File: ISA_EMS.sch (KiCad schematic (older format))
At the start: 60 parts, among them J1 ISA BUS, J2 EMS Address, J3 ROM Config, U1 74HCT688, U10 74HCT32, U11 74HCT04, U12 74ACT245, U13 AS6C4008-55PCN, U14 AS6C4008-55PCN, U15 AS6C4008-55PCN, U16 AS6C4008-55PCN, U17 74HCT138, U18 74LS573, U19 74LS573, U2 SST39SF040, U20 74LS573, U21 74LS573, U3 AS6C4008-55PCN, U4 AS6C4008-55PCN, U5 AS6C4008-55PCN, U6 AS6C4008-55PCN, U7 74HCT688, U8 74HCT688, U9 74HCT139

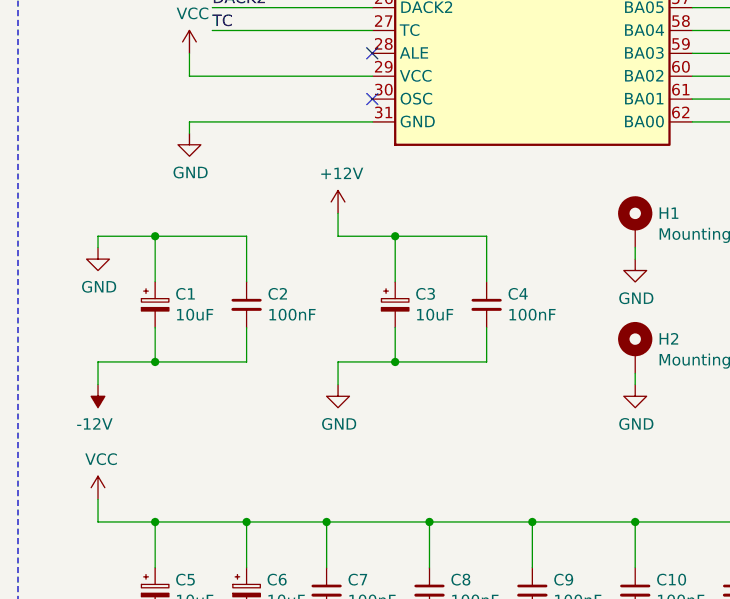
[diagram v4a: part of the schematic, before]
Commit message: Routed the board
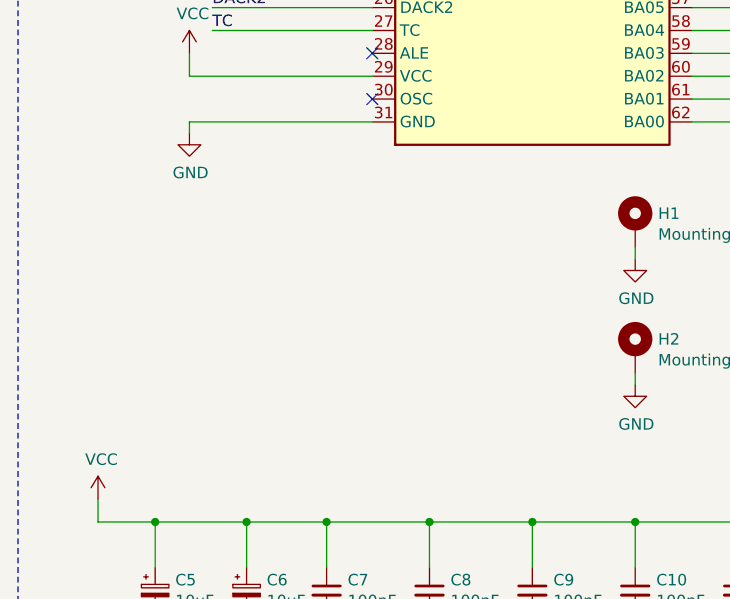
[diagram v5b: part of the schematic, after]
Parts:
- removed C1, C3: 10uF, Capacitor_THT:CP_Radial_D5.0mm_P2.50mm, symbol Device:CP_Small
- removed C2, C4: 100nF, Capacitor_THT:C_Disc_D6.0mm_W2.5mm_P5.00mm, symbol Device:C_Small
- H1, H2: footprint (none) -> skiselev_footprints:Hole_3mm
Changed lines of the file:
@@
 	1500 9250 2300 9250
 $Comp
-L Device:CP_Small C1
-U 1 1 610853FE
-P 1350 10250
-F 0 "C1" H 1438 10296 50  0000 L CNN
-F 1 "10uF" H 1438 10205 50  0000 L CNN
-F 2 "Capacitor_THT:CP_Radial_D5.0mm_P2.50mm" H 1350 10250 50  0001 C CNN
-F 3 "~" H 1350 10250 50  0001 C CNN
-	1    1350 10250
-	1    0    0    -1
-$EndComp
-$Comp
-L Device:C_Small C2
-U 1 1 61086024
-P 1750 10250
-F 0 "C2" H 1842 10296 50  0000 L CNN
-F 1 "100nF" H 1842 10205 50  0000 L CNN
-F 2 "Capacitor_THT:C_Disc_D6.0mm_W2.5mm_P5.00mm" H 1750 10250 50  0001 C CNN
-F 3 "~" H 1750 10250 50  0001 C CNN
-	1    1750 10250
-	1    0    0    -1
-$EndComp
-$Comp
-L power:GND #PWR0135
-U 1 1 6108687E
-P 1100 10000
-F 0 "#PWR0135" H 1100 9750 50  0001 C CNN
-F 1 "GND" H 1105 9827 50  0000 C CNN
-F 2 "" H 1100 10000 50  0001 C CNN
-F 3 "" H 1100 10000 50  0001 C CNN
-	1    1100 10000
-	1    0    0    -1
-$EndComp
-Wire Wire Line
-	1100 10000 1100 9950
-Wire Wire Line
-	1100 9950 1350 9950
-Wire Wire Line
-	1350 9950 1350 10150
-Wire Wire Line
-	1350 9950 1750 9950
-Wire Wire Line
-	1750 9950 1750 10150
-Connection ~ 1350 9950
-$Comp
-L power:-12V #PWR0136
-U 1 1 610C70C1
-P 1100 10600
-F 0 "#PWR0136" H 1100 10700 50  0001 C CNN
-F 1 "-12V" H 1115 10773 50  0000 C CNN
-F 2 "" H 1100 10600 50  0001 C CNN
-F 3 "" H 1100 10600 50  0001 C CNN
-	1    1100 10600
-	-1   0    0    1
-$EndComp
-Wire Wire Line
-	1750 10500 1350 10500
-Wire Wire Line
-	1350 10500 1350 10350
-Wire Wire Line
-	1750 10350 1750 10500
-Wire Wire Line
-	1350 10500 1100 10500
-Wire Wire Line
-	1100 10500 1100 10600
-Connection ~ 1350 10500
-$Comp
-L Device:CP_Small C3
-U 1 1 6116AF87
-P 2400 10250
-F 0 "C3" H 2488 10296 50  0000 L CNN
-F 1 "10uF" H 2488 10205 50  0000 L CNN
-F 2 "Capacitor_THT:CP_Radial_D5.0mm_P2.50mm" H 2400 10250 50  0001 C CNN
-F 3 "~" H 2400 10250 50  0001 C CNN
-	1    2400 10250
-	1    0    0    -1
-$EndComp
-$Comp
-L Device:C_Small C4
-U 1 1 6116B0B7
-P 2800 10250
-F 0 "C4" H 2892 10296 50  0000 L CNN
-F 1 "100nF" H 2892 10205 50  0000 L CNN
-F 2 "Capacitor_THT:C_Disc_D6.0mm_W2.5mm_P5.00mm" H 2800 10250 50  0001 C CNN
-F 3 "~" H 2800 10250 50  0001 C CNN
-	1    2800 10250
-	1    0    0    -1
-$EndComp
-$Comp
-L power:GND #PWR0137
-U 1 1 6116B0C1
-P 2150 10600
-F 0 "#PWR0137" H 2150 10350 50  0001 C CNN
-F 1 "GND" H 2155 10427 50  0000 C CNN
-F 2 "" H 2150 10600 50  0001 C CNN
-F 3 "" H 2150 10600 50  0001 C CNN
-	1    2150 10600
-	1    0    0    -1
-$EndComp
-Wire Wire Line
-	2400 9950 2400 10150
-Wire Wire Line
-	2400 9950 2800 9950
-Wire Wire Line
-	2800 9950 2800 10150
-Wire Wire Line
-	2800 10500 2400 10500
-Wire Wire Line
-	2400 10500 2400 10350
-Wire Wire Line
-	2800 10350 2800 10500
-Wire Wire Line
-	2400 10500 2150 10500
-Wire Wire Line
-	2150 10500 2150 10600
-Connection ~ 2400 10500
-Wire Wire Line
-	2400 9950 2150 9950
-Connection ~ 2400 9950
-Wire Wire Line
-	2150 9850 2150 9950
-$Comp
-L power:+12V #PWR0138
-U 1 1 61240CC5
-P 2150 9850
-F 0 "#PWR0138" H 2150 9700 50  0001 C CNN
-F 1 "+12V" H 2165 10023 50  0000 C CNN
-F 2 "" H 2150 9850 50  0001 C CNN
-F 3 "" H 2150 9850 50  0001 C CNN
-	1    2150 9850
-	1    0    0    -1
-$EndComp
-$Comp
 L Device:CP_Small C5
 U 1 1 61243061
@@
 F 0 "H1" H 3550 9949 50  0000 L CNN
 F 1 "MountingHole_Pad" H 3550 9858 50  0000 L CNN
-F 2 "" H 3450 9900 50  0001 C CNN
+F 2 "skiselev_footprints:Hole_3mm" H 3450 9900 50  0001 C CNN
 F 3 "~" H 3450 9900 50  0001 C CNN
 	1    3450 9900
@@
 F 0 "H2" H 3550 10499 50  0000 L CNN
 F 1 "MountingHole_Pad" H 3550 10408 50  0000 L CNN
-F 2 "" H 3450 10450 50  0001 C CNN
+F 2 "skiselev_footprints:Hole_3mm" H 3450 10450 50  0001 C CNN
 F 3 "~" H 3450 10450 50  0001 C CNN
 	1    3450 10450
@@
 $EndComp
 $Comp
-L power:GND #PWR?
+L power:GND #PWR0173
 U 1 1 60A008FD
 P 3450 10050
-F 0 "#PWR?" H 3450 9800 50  0001 C CNN
+F 0 "#PWR0173" H 3450 9800 50  0001 C CNN
 F 1 "GND" H 3455 9877 50  0000 C CNN
 F 2 "" H 3450 10050 50  0001 C CNN
@@
 $EndComp
 $Comp
-L power:GND #PWR?
+L power:GND #PWR0174
 U 1 1 60A01C8A
 P 3450 10600
-F 0 "#PWR?" H 3450 10350 50  0001 C CNN
+F 0 "#PWR0174" H 3450 10350 50  0001 C CNN
 F 1 "GND" H 3455 10427 50  0000 C CNN
 F 2 "" H 3450 10600 50  0001 C CNN

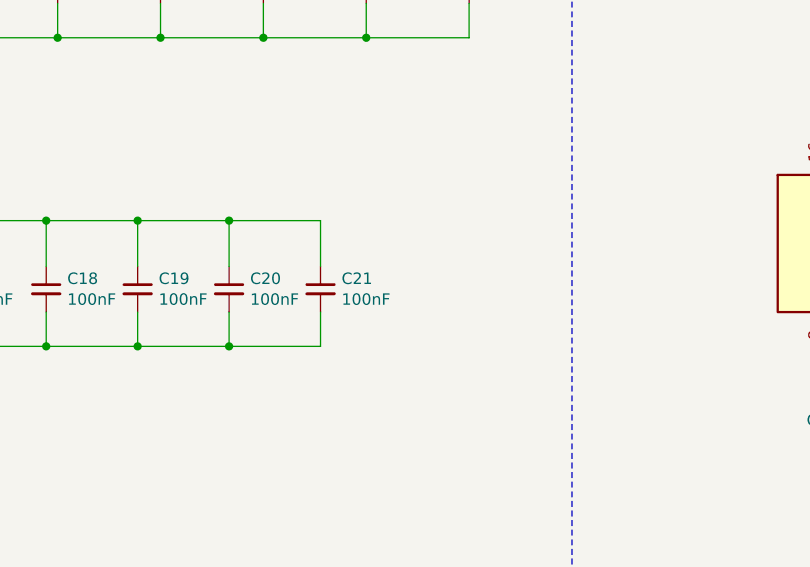
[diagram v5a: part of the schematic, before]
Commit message: Added missing cap
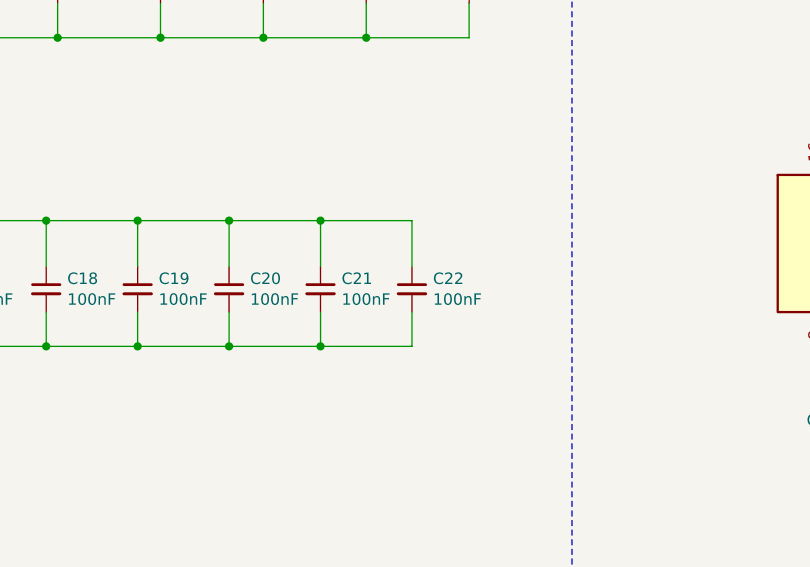
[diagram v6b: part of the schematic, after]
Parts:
- added C22: 100nF, Capacitor_THT:C_Disc_D6.0mm_W2.5mm_P5.00mm, symbol Device:C_Small
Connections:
- net GND: now also C22.2
- net VCC: now also C22.1
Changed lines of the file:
@@
 Wire Wire Line
 	3450 10050 3450 10000
+$Comp
+L Device:C_Small C22
+U 1 1 6073A804
+P 4250 14150
+F 0 "C22" H 4342 14196 50  0000 L CNN
+F 1 "100nF" H 4342 14105 50  0000 L CNN
+F 2 "Capacitor_THT:C_Disc_D6.0mm_W2.5mm_P5.00mm" H 4250 14150 50  0001 C CNN
+F 3 "~" H 4250 14150 50  0001 C CNN
+	1    4250 14150
+	1    0    0    -1
+$EndComp
+Wire Wire Line
+	3850 13850 4250 13850
+Wire Wire Line
+	4250 13850 4250 14050
+Connection ~ 3850 13850
+Wire Wire Line
+	3850 14400 4250 14400
+Wire Wire Line
+	4250 14400 4250 14250
+Connection ~ 3850 14400
 $EndSCHEMATC

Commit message: Add notes to schematics
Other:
- note added: "Bus Transceiver"
- note added: "Data Buffer"
- note added: "RAM"
- note added: "Register Address Decode"
- note added: "SRAM Chip Select"
- moved on the sheet: D1, R3, U17, U18, U19, U20, U21

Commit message: Removed BOOTROM, make board smaller, reroute
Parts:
- removed C19, C20: 100nF, Capacitor_THT:C_Disc_D6.0mm_W2.5mm_P5.00mm, symbol Device:C_Small
- removed J3: ROM Config, Connector_PinHeader_2.54mm:PinHeader_2x07_P2.54mm_Vertical, symbol Connector_Generic:Conn_02x07_Odd_Even
- removed R1, R2: 10k, Resistor_THT:R_Axial_DIN0207_L6.3mm_D2.5mm_P10.16mm_Horizontal, symbol Device:R_Small
- removed RN1: 10k, Resistor_THT:R_Array_SIP6, symbol Device:R_Network05
- removed U1: 74HCT688, Package_DIP:DIP-20_W7.62mm_LongPads, symbol 74xx:74HCT688
- removed U2: SST39SF040, Package_DIP:DIP-32_W15.24mm_LongPads, symbol Memory_Flash:SST39SF040
- R3: value 1k -> 470
- U12: value 74ACT245 -> 74LS245
- U18, U19, U20, U21: value 74LS573 -> 74HCT573
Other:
- note removed: "32K"
- note removed: "32K ROM bank"
- note removed: "64K"
- note removed: "64K ROM bank"
- note removed: "A000h"
- note removed: "A15"
- note removed: "A16"
- note removed: "A17"
- note removed: "A18"
- note removed: "A800h"
- note removed: "B000h"
- note removed: "B800h"
- note removed: "C000h"
- note removed: "C800h"
- note removed: "D000h"
- note removed: "D800h"
- note removed: "E000h"
- note removed: "E800h"
- note removed: "ENA"
- note removed: "F000h"
- note removed: "F800h"
- note removed: "If 32K mode is set, the A15 line will\nnot be used to address the content\nof the ROM (FLASH_A15 will be always\nlow), but will be decoded by the\n'688 to decide whether the ROM gets\nenabled or not.\n\nIn 64K mode, the A15 line will be used\nto address the content of the ROM,\nthe A15 jumper MUST be set, otherwise\nthe decoder will fail to enable the ROM\n(note how the COMPARATOR_A15 line\nwill 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"
- note removed: "Jumper ONE of these two to\nselect 32K or 64K ROM slot size"
- note removed: "Jumper to ENABLE the ROM"
- note removed: "Logic taken from https://www.lo-tech.co.uk/wiki/Lo-tech_ISA_ROM_Board"
- note removed: "ROM"
- note removed: "Remember that the comparator is\nhardwired to check for A19 to be HIGH!"
- note removed: "X"
